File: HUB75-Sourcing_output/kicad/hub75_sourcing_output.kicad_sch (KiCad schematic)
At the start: 7 parts, among them J13 Screw_Terminal_01x02, Q13 AO3401A

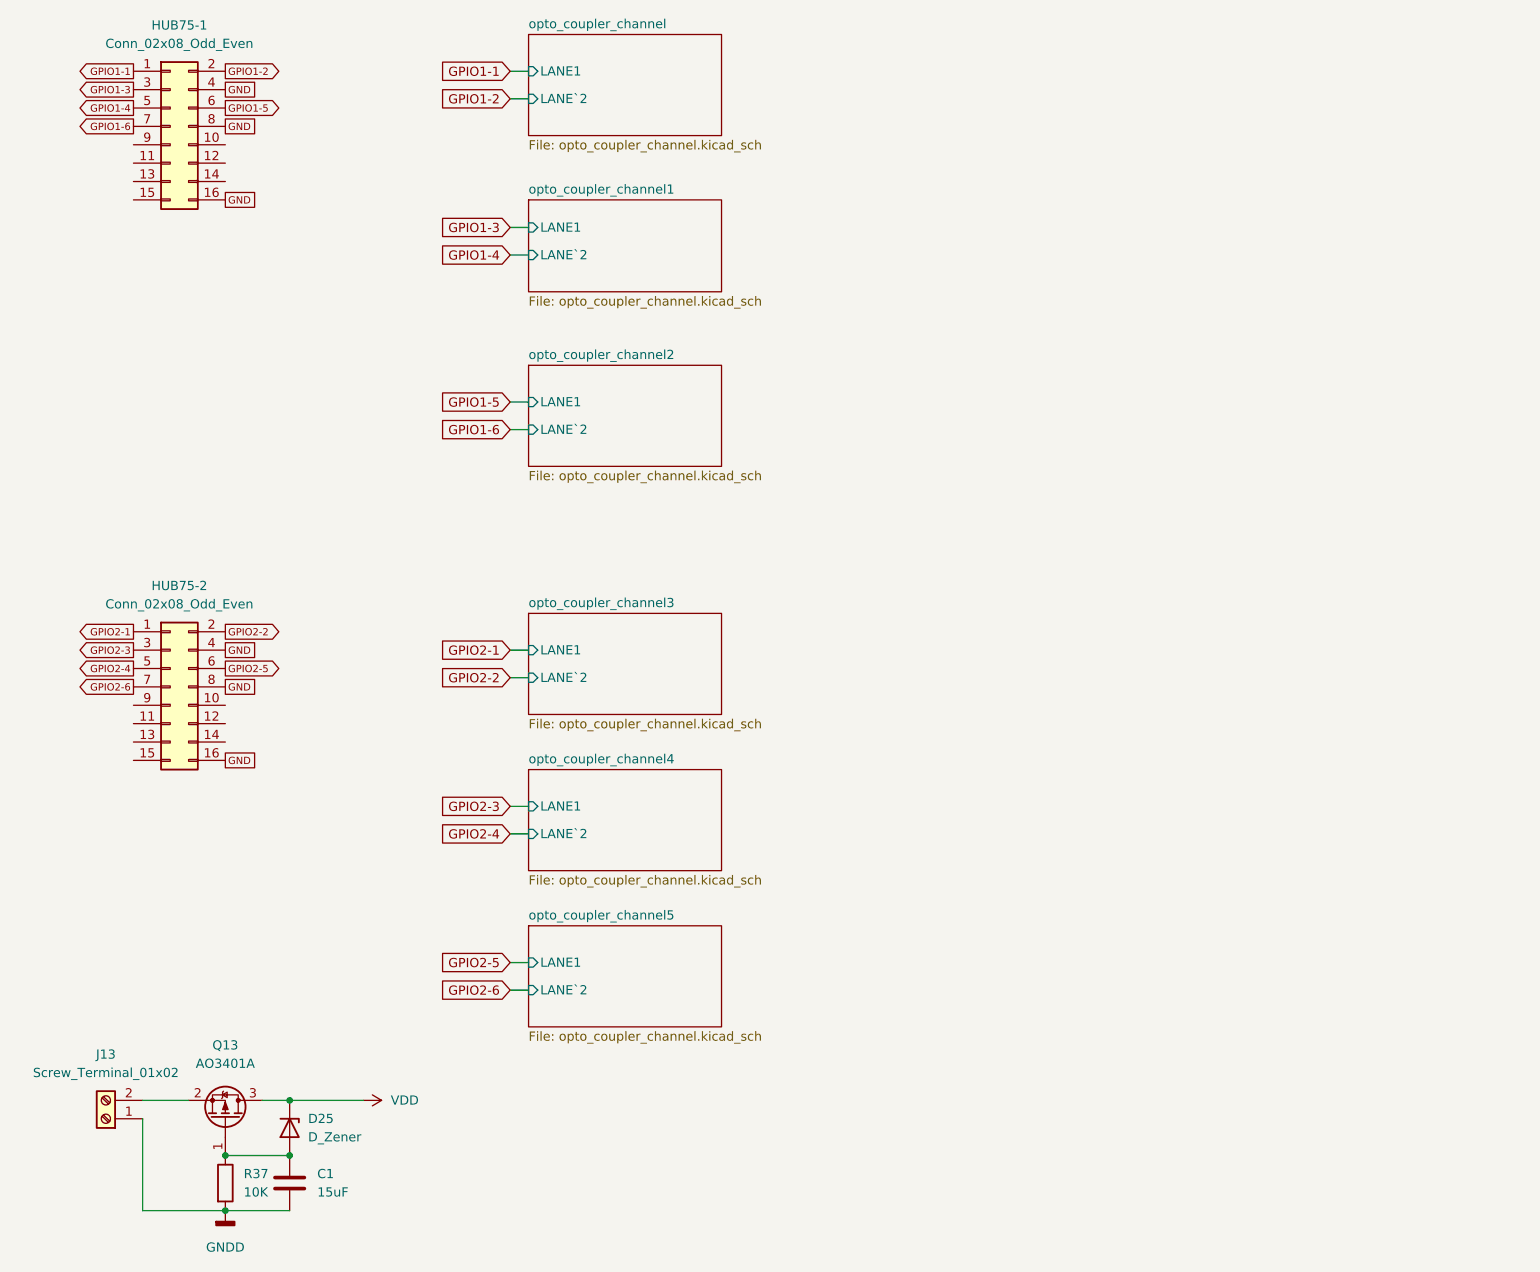
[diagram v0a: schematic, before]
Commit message: Update board with current mirror + backup
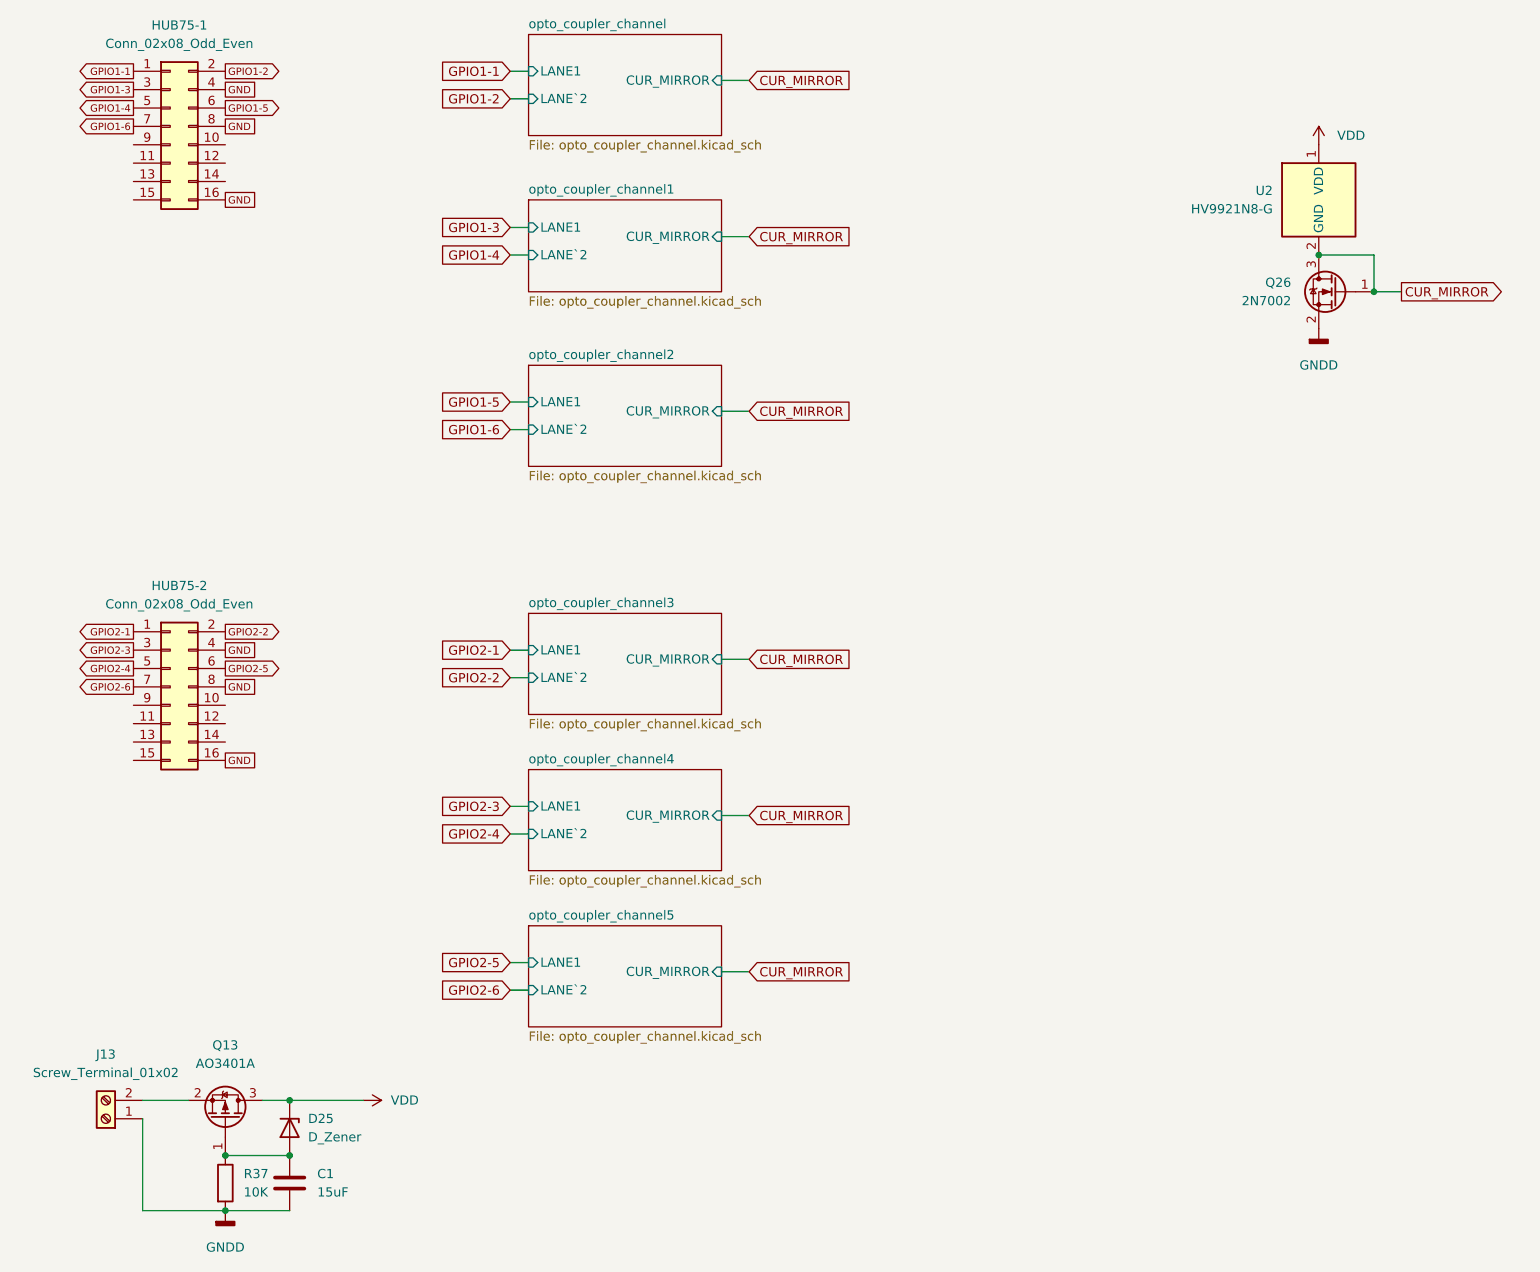
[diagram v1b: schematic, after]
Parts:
- added Q26: 2N7002, Package_TO_SOT_SMD:SOT-23, symbol Transistor_FET:2N7002
- added U2: HV9921N8-G, Package_TO_SOT_SMD:SOT-89-3, symbol Driver_LED:HV9921N8-G
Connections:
- net GNDD: now also Q26.2 (S)
- net VDD: now also U2.1 (VDD)
- new net CUR_MIRROR: Q26.1 (G), Q26.3 (D), U2.2 (GND)
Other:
- sheet opto_coupler_channel ports: added CUR_MIRROR; removed none
- sheet opto_coupler_channel1 ports: added CUR_MIRROR; removed none
- sheet opto_coupler_channel2 ports: added CUR_MIRROR; removed none
- sheet opto_coupler_channel3 ports: added CUR_MIRROR; removed none
- sheet opto_coupler_channel4 ports: added CUR_MIRROR; removed none
- sheet opto_coupler_channel5 ports: added CUR_MIRROR; removed none

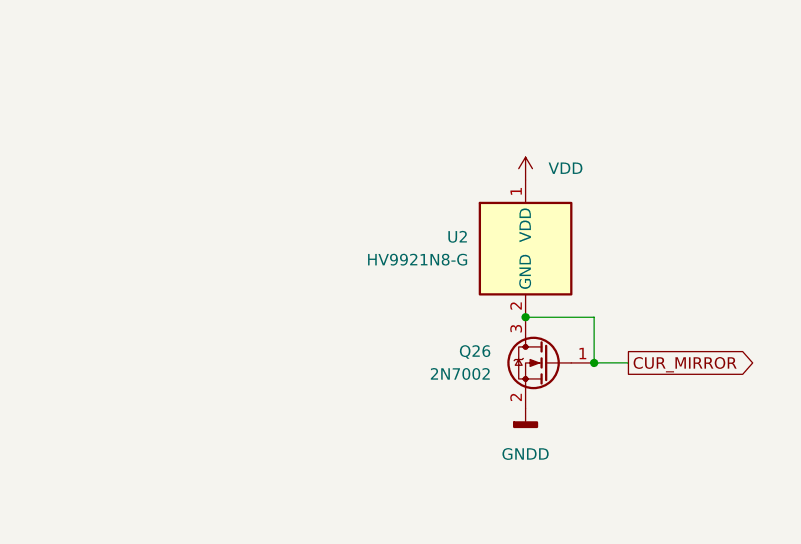
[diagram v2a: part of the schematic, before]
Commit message: Update part number
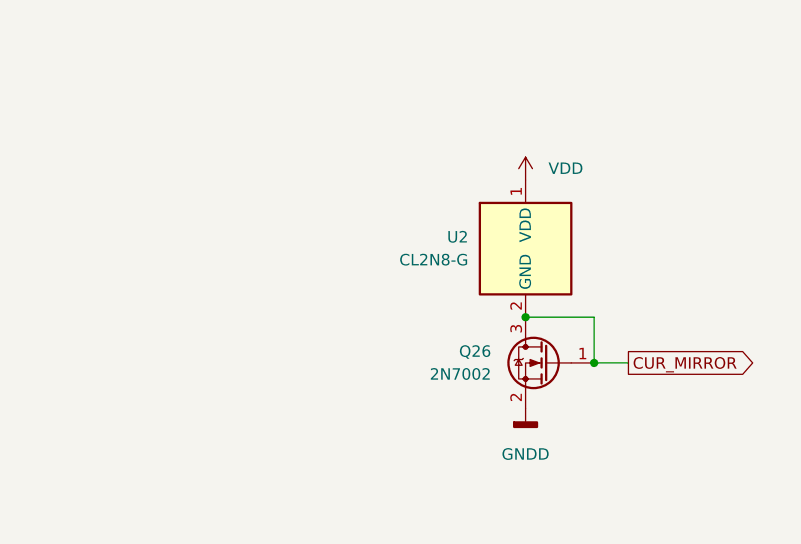
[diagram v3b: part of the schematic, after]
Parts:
- U2: value HV9921N8-G -> CL2N8-G
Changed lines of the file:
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@@
       (effects (font (size 1.27 1.27)) (justify right))
     )
-    (property "Value" "HV9921N8-G" (id 1) (at 187.96 52.0699 0)
+    (property "Value" "CL2N8-G" (id 1) (at 187.96 52.0699 0)
       (effects (font (size 1.27 1.27)) (justify right))
     )
@@
       (effects (font (size 1.27 1.27)) (justify left) hide)
     )
-    (property "Datasheet" "http://ww1.microchip.com/downloads/en/DeviceDoc/20005311A.pdf" (id 3) (at 194.31 50.8 0)
+    (property "Datasheet" "https://cdn-reichelt.de/documents/datenblatt/A200/CL2_DS.pdf" (id 3) (at 194.31 50.8 0)
       (effects (font (size 1.27 1.27)) hide)
     )
@@
     )
     (path "/46d510fa-9c5c-43d0-a15e-4989c5c3c096"
-      (reference "U2") (unit 1) (value "HV9921N8-G") (footprint "Package_TO_SOT_SMD:SOT-89-3")
+      (reference "U2") (unit 1) (value "CL2N8-G") (footprint "Package_TO_SOT_SMD:SOT-89-3")
     )
     (path "/b97ce019-f40c-494d-a8f2-c1e1e7770eda/efa18901-dd65-4597-9399-7e85f1015b89"

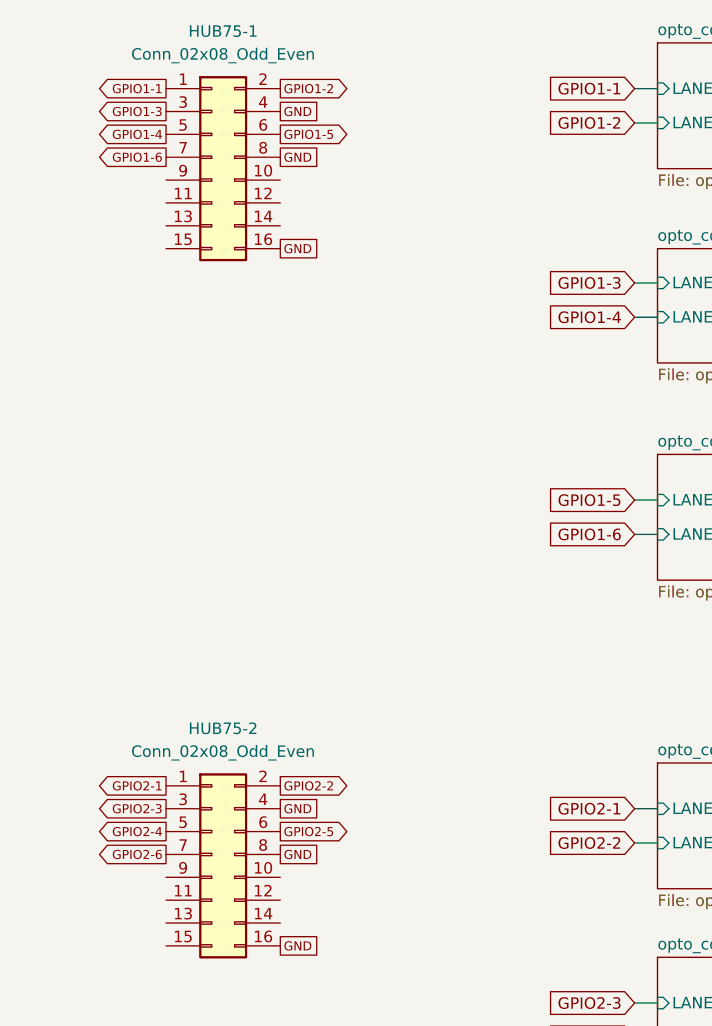
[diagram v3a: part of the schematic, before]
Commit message: Remove incorrect GND connection
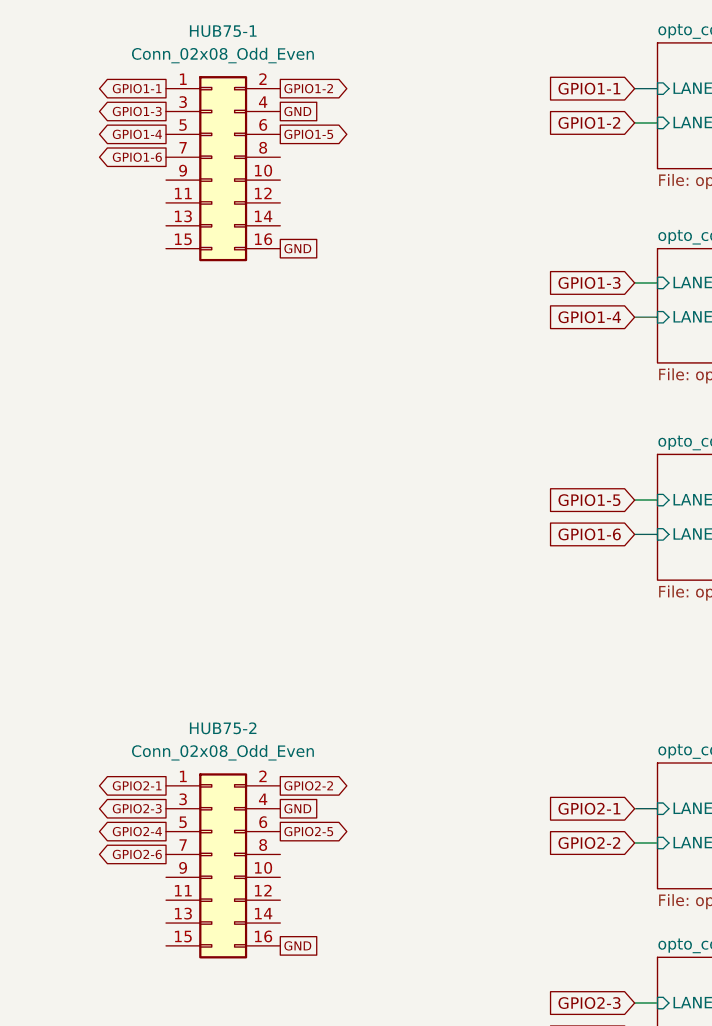
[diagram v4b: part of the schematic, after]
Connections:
- net GND: no longer HUB75-1.8 (Pin_8), HUB75-2.8 (Pin_8)
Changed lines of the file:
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@@
-    )
-  )
-  (global_label "GND" (shape passive) (at 43.18 118.11 0) (fields_autoplaced)
-    (effects (font (size 1 1)) (justify left))
-    (property "Intersheet References" "${INTERSHEET_REFS}" (id 0) (at 48.1276 118.0475 0)
-      (effects (font (size 1 1)) (justify left) hide)
     )
   )
@@
     )
   )
-  (global_label "GND" (shape passive) (at 43.18 40.64 0) (fields_autoplaced)
-    (effects (font (size 1 1)) (justify left))
-    (property "Intersheet References" "${INTERSHEET_REFS}" (id 0) (at 48.1276 40.5775 0)
-      (effects (font (size 1 1)) (justify left) hide)
-    )
-  )
   (global_label "GPIO1-1" (shape output) (at 30.48 33.02 180) (fields_autoplaced)
     (effects (font (size 1 1)) (justify right))
@@
       (effects (font (size 1.27 1.27)) hide)
     )
+    (pin "1")
     (pin "2")
-    (pin "1")
   )
   (symbol (lib_id "Transistor_FET:2N7002") (at 196.85 63.5 0) (mirror y) (unit 1)
